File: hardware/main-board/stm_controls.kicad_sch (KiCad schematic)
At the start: 24 parts, among them SW1 SW_SPST, U1 74HC164, U10 MT8816AF1, U11 MT8816AF1, U12 MT8816AF1, U13 AD5263BRUZ200, U14 AD5263BRUZ200, U15 AD5263BRUZ200, U16 AD5263BRUZ200, U17 AD5263BRUZ200, U18 AD5263BRUZ200, U19 AD5263BRUZ200, U2 74HC164, U20 AD5263BRUZ200, U22 STM32F091RCTx, U23 FT232RL, U3 74HC164, U4 MT8816AF1, U5 MT8816AF1, U6 MT8816AF1, U7 MT8816AF1, U8 MT8816AF1, U9 MT8816AF1

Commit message: God is Real, God is Real, Im not kidding this time I wouldn't joke about this
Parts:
- added C1, C10: 10µF, symbol Device:C
- added C2, C3, C4, C5, C9: 100nF, symbol Device:C
- added C6: 10nF, symbol Device:C
- added C7, C8: 1µF, symbol Device:C
- added F1: 500mA, symbol Device:Fuse
- added FB1: 120R, symbol Device:FerriteBead
- added J1: Conn_02x05_Odd_Even, symbol Connector_Generic:Conn_02x05_Odd_Even
- added J2: USB_C_Receptacle_USB2.0_14P, symbol Connector:USB_C_Receptacle_USB2.0_14P
- added J3: Conn_01x02_Pin, symbol Connector:Conn_01x02_Pin
- added R2: 1kΩ, symbol Device:R_US
- added R3: 5.1kΩ, symbol Device:R_US
- added R4: R_US, symbol Device:R_US
- added SW1: SW_SPST, symbol Switch:SW_SPST
- R1: value R_US -> 1kΩ
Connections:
- net GND: now also SW1.1 (A), U22.12 (VSSA), U22.18 (VSS), U22.31 (VSS), U22.47 (VSS), U22.63 (VSS), U23.25 (AGND), C1.2, C10.2, C2.2, C3.2, C4.2, C5.2, C6.2, C7.2, C8.2, C9.2, J1.3 (Pin_3), J1.4 (Pin_4), J2.A1 (GND), J2.A12 (GND), J2.B1 (GND), J2.B12 (GND), J2.S1 (SHIELD), R2.2, R3.2, R4.2; no longer R1.1
- net at U23.15 (USBD+): now also J2.A6 (D+), J2.B6 (D+)
- net at U23.16 (USBD-): now also J2.A7 (D-), J2.B7 (D-)
- net +3.3V: now reaches U23.4 (VCCIO)
- net +3.3V: now also R1.1, U22.1 (VBAT), U22.19 (VDD), U22.32 (VDD), U22.48 (VDDIO2), U22.64 (VDD), C1.1, C2.1, C3.1, C4.1, C5.1, C8.1, FB1.2, J1.7 (Pin_7), J1.8 (Pin_8), SW1.1 (A)
- net +3.3VA: now reaches U22.13 (VDDA)
- net +3.3VA: now also C6.1, C7.1, FB1.1
- net XOSC_IN: now reaches U22.3 (PC14)
- net XOSC_IN: now also J3.2 (Pin_2)
- net XOSC_OUT: now reaches U22.4 (PC15)
- net XOSC_OUT: now also J3.1 (Pin_1)
- net SWDIO: now reaches U22.46 (PA13)
- net SWDIO: now also J1.2 (Pin_2)
- net SWCLK: now reaches U22.49 (PA14)
- net SWCLK: now also J1.6 (Pin_6)
- net at U22.60 (PF11): now also R2.1, SW1.2 (B)
- net +3V3: no longer names the net of U23.20 (VCC)
- net +3V3: now also C10.1, C9.1, F1.2; no longer SW1.1 (A)
- new net: J2.A5 (CC1), R3.1
- new net: J2.B5 (CC2), R4.1
- new net: F1.1, J2.A4 (VBUS), J2.A9 (VBUS), J2.B4 (VBUS), J2.B9 (VBUS)
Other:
- moved on the sheet: SW1, U22, U23

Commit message: fortnite info cache
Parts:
- renumbered C10 to C20, C1 to C21, C9 to C22, C2 to C23, C3 to C24, C4 to C25, C5 to C26, C6 to C27, C7 to C28, C8 to C29, F1 to F3, J1 to J10, J3 to J11, J2 to J9, R3 to R1, R4 to R2, R1 to R3, R2 to R4, SW1 to SW3, SW1 to SW4, U10 to U1, U17 to U14, U18 to U15, U4 to U17, U5 to U18, U14 to U20, U16 to U21, U6 to U23, U7 to U24, U19 to U26, U20 to U27, U8 to U29, U9 to U30, U1 to U33, U23 to U34, U2 to U35, U22 to U36, U3 to U37, U13 to U8, U15 to U9

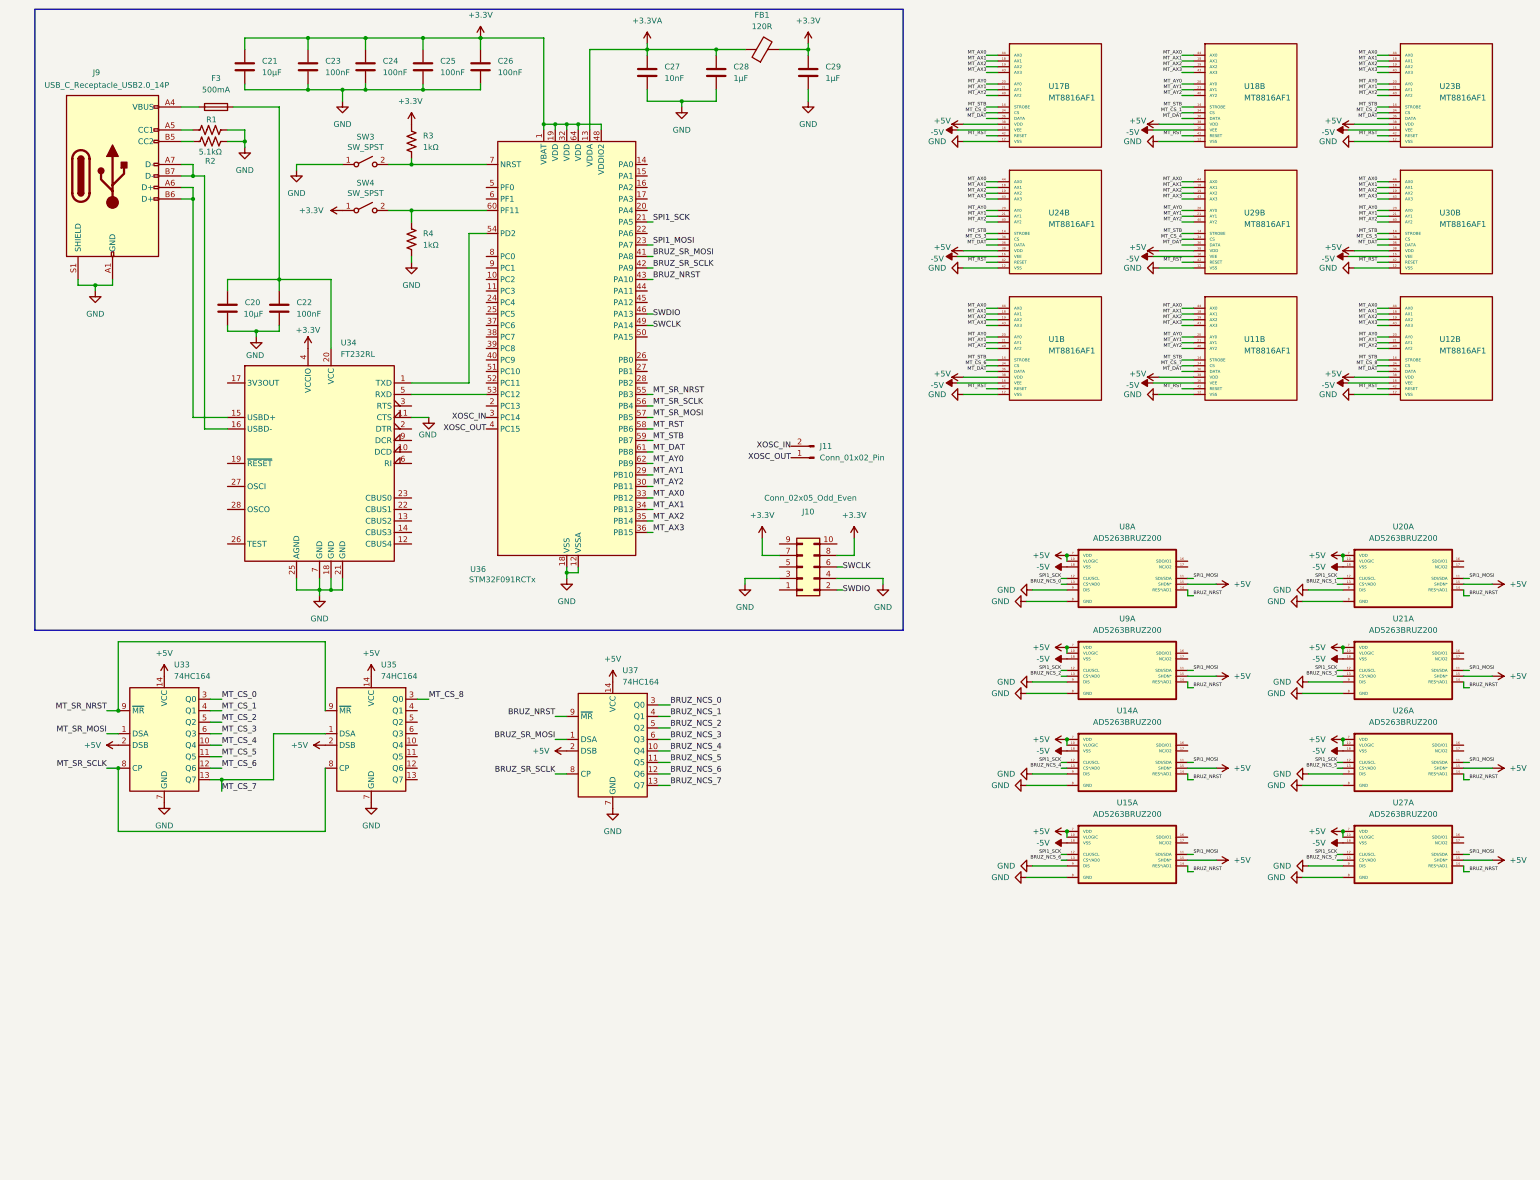
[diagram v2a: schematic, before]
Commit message: Updated Footprints and Controls
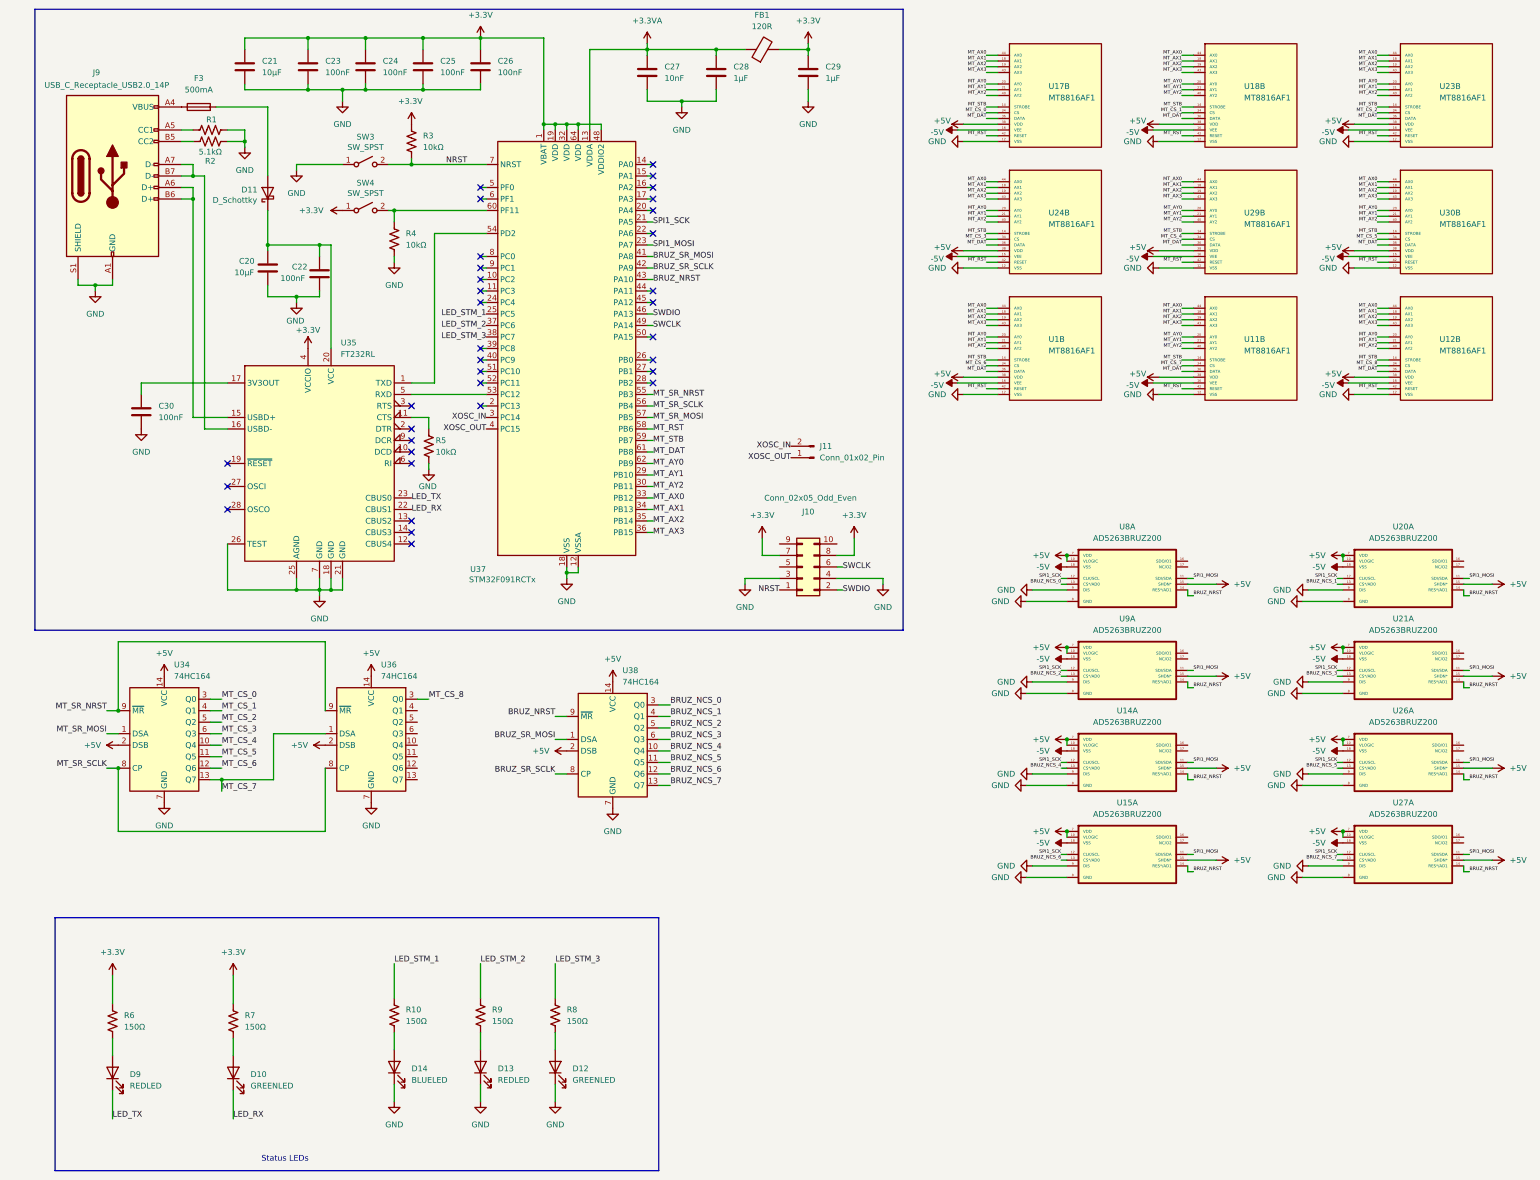
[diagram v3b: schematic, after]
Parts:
- added C30: 100nF, symbol Device:C
- added D10, D12: GREENLED, symbol Device:LED
- added D11: D_Schottky, symbol Device:D_Schottky
- added D13, D9: REDLED, symbol Device:LED
- added D14: BLUELED, symbol Device:LED
- added R10, R6, R7, R8, R9: 150Ω, symbol Device:R_US
- added R5: 10kΩ, symbol Device:R_US
- C20, C21, C22, C23, C24, C25, C26, C27, C28, C29: footprint (none) -> Capacitor_SMD:C_0603_1608Metric_Pad1.08x0.95mm_HandSolder
- F3: footprint (none) -> Fuse:Fuse_0603_1608Metric_Pad1.05x0.95mm_HandSolder
- FB1: footprint (none) -> Inductor_SMD:L_0603_1608Metric_Pad1.05x0.95mm_HandSolder
- J9: footprint (none) -> Connector_USB:USB_C_Receptacle_G-Switch_GT-USB-7010ASV
- R1, R2: footprint (none) -> Resistor_SMD:R_0603_1608Metric_Pad0.98x0.95mm_HandSolder
- R3, R4: value 1kΩ -> 10kΩ; footprint (none) -> Resistor_SMD:R_0603_1608Metric_Pad0.98x0.95mm_HandSolder
- U14, U15, U20, U21, U26, U27, U8, U9: footprint AD5263BRUZ200:SOP65P640X120-24N -> SeniorDesignFP:SOP65P640X120-24N
- U34: renamed from U33; footprint (none) -> Package_SO:SOIC-14_3.9x8.7mm_P1.27mm
- U36: renamed from U35; footprint (none) -> Package_SO:SOIC-14_3.9x8.7mm_P1.27mm
- U38: renamed from U37; footprint (none) -> Package_SO:SOIC-14_3.9x8.7mm_P1.27mm
- renumbered U34 to U35, U36 to U37
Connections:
- net +3.3V: now also R6.1, R7.1
- net GND: now also U35.26 (TEST), C30.2, D12.1 (K), D13.1 (K), D14.1 (K), R5.2; no longer U35.11 (CTS)
- net at C20.1, C22.1, U35.20 (VCC): now also D11.1 (K); no longer F3.2
- net NRST: now reaches R3.2, SW3.2 (B), U37.7 (NRST)
- net NRST: now also J10.1 (Pin_1)
- net at U35.17 (3V3OUT): now also C30.1
- net LED_RX: now reaches U35.22 (CBUS1)
- net LED_RX: now also D10.1 (K)
- net LED_TX: now reaches U35.23 (CBUS0)
- net LED_TX: now also D9.1 (K)
- net LED_STM_1: now reaches U37.25 (PC5)
- net LED_STM_1: now also R10.1
- net LED_STM_2: now reaches U37.37 (PC6)
- net LED_STM_2: now also R9.1
- net LED_STM_3: now reaches U37.38 (PC7)
- net LED_STM_3: now also R8.1
- new net: R5.1, U35.11 (CTS)
- new net: D11.2 (A), F3.2
- new net: D13.2 (A), R9.2
- new net: D10.2 (A), R7.2
- new net: D9.2 (A), R6.2
- new net: D12.2 (A), R8.2
- new net: D14.2 (A), R10.2
- no-connect marks 0 -> 35
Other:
- note added: "Status LEDs"
- moved on the sheet: C20, C22, F3, R4

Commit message: Designated majority of footprints
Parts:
- C30: footprint (none) -> Capacitor_SMD:C_0603_1608Metric_Pad1.08x0.95mm_HandSolder
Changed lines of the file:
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@@
 			)
 		)
-		(property "Footprint" ""
+		(property "Footprint" "Capacitor_SMD:C_0603_1608Metric_Pad1.08x0.95mm_HandSolder"
 			(at 46.6852 105.41 0)
 			(effects

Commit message: Fully filled footprints
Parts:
- D10, D12, D13, D14, D9: footprint (none) -> Diode_SMD:D_0805_2012Metric_Pad1.15x1.40mm_HandSolder
- D11: footprint (none) -> Diode_SMD:D_SOD-123
- J10: footprint (none) -> Connector_PinHeader_1.00mm:PinHeader_2x05_P1.00mm_Horizontal
- J11: footprint (none) -> Connector_PinHeader_1.00mm:PinHeader_1x02_P1.00mm_Horizontal
- R10, R5, R6, R7, R8, R9: footprint (none) -> Resistor_SMD:R_0603_1608Metric_Pad0.98x0.95mm_HandSolder
- SW3, SW4: footprint (none) -> Button_Switch_SMD:SW_SPST_B3U-1100P
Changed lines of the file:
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@@
 			)
 		)
-		(property "Footprint" ""
+		(property "Footprint" "Resistor_SMD:R_0603_1608Metric_Pad0.98x0.95mm_HandSolder"
 			(at 110.236 109.474 90)
 			(effects
@@
 			)
 		)
-		(property "Footprint" ""
+		(property "Footprint" "Diode_SMD:D_SOD-123"
 			(at 73.66 53.34 0)
 			(effects
@@
 			)
 		)
-		(property "Footprint" ""
+		(property "Footprint" "Diode_SMD:D_0805_2012Metric_Pad1.15x1.40mm_HandSolder"
 			(at 120.65 246.38 0)
 			(effects
@@
 			)
 		)
-		(property "Footprint" ""
+		(property "Footprint" "Button_Switch_SMD:SW_SPST_B3U-1100P"
 			(at 95.25 57.15 0)
 			(effects
@@
 			)
 		)
-		(property "Footprint" ""
+		(property "Footprint" "Resistor_SMD:R_0603_1608Metric_Pad0.98x0.95mm_HandSolder"
 			(at 67.056 236.474 90)
 			(effects
@@
 			)
 		)
-		(property "Footprint" ""
+		(property "Footprint" "Button_Switch_SMD:SW_SPST_B3U-1100P"
 			(at 95.25 46.99 0)
 			(effects
@@
 			)
 		)
-		(property "Footprint" ""
+		(property "Footprint" "Diode_SMD:D_0805_2012Metric_Pad1.15x1.40mm_HandSolder"
 			(at 39.37 247.65 0)
 			(effects
@@
 			)
 		)
-		(property "Footprint" ""
+		(property "Footprint" "Diode_SMD:D_0805_2012Metric_Pad1.15x1.40mm_HandSolder"
 			(at 137.16 246.38 0)
 			(effects
@@
 			)
 		)
-		(property "Footprint" ""
+		(property "Footprint" "Diode_SMD:D_0805_2012Metric_Pad1.15x1.40mm_HandSolder"
 			(at 101.6 246.38 0)
 			(effects
@@
 			)
 		)
-		(property "Footprint" ""
+		(property "Footprint" "Resistor_SMD:R_0603_1608Metric_Pad0.98x0.95mm_HandSolder"
 			(at 40.386 236.474 90)
 			(effects
@@
 			)
 		)
-		(property "Footprint" ""
+		(property "Footprint" "Resistor_SMD:R_0603_1608Metric_Pad0.98x0.95mm_HandSolder"
 			(at 102.616 235.204 90)
 			(effects
@@
 			)
 		)
-		(property "Footprint" ""
+		(property "Footprint" "Connector_PinHeader_1.00mm:PinHeader_2x05_P1.00mm_Horizontal"
 			(at 191.77 135.89 0)
 			(effects
@@
 			)
 		)
-		(property "Footprint" ""
+		(property "Footprint" "Resistor_SMD:R_0603_1608Metric_Pad0.98x0.95mm_HandSolder"
 			(at 138.176 235.204 90)
 			(effects
@@
 			)
 		)
-		(property "Footprint" ""
+		(property "Footprint" "Resistor_SMD:R_0603_1608Metric_Pad0.98x0.95mm_HandSolder"
 			(at 121.666 235.204 90)
 			(effects
@@
 			)
 		)
-		(property "Footprint" ""
+		(property "Footprint" "Connector_PinHeader_1.00mm:PinHeader_1x02_P1.00mm_Horizontal"
 			(at 194.31 111.76 0)
 			(effects
@@
 			)
 		)
-		(property "Footprint" ""
+		(property "Footprint" "Diode_SMD:D_0805_2012Metric_Pad1.15x1.40mm_HandSolder"
 			(at 66.04 247.65 0)
 			(effects

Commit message: PCB comps in, and formatted
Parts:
- U1, U11, U12, U17, U18, U23, U24, U29, U30: footprint MT8816AF1:QFP80P1200X1200X120-44N -> SeniorDesignFP:QFP80P1200X1200X120-44N
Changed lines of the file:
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@@
 			)
 		)
-		(property "Footprint" "MT8816AF1:QFP80P1200X1200X120-44N"
+		(property "Footprint" "SeniorDesignFP:QFP80P1200X1200X120-44N"
 			(at 272.034 115.062 0)
 			(effects
@@
 			)
 		)
-		(property "Footprint" "MT8816AF1:QFP80P1200X1200X120-44N"
+		(property "Footprint" "SeniorDesignFP:QFP80P1200X1200X120-44N"
 			(at 358.394 115.062 0)
 			(effects
@@
 			)
 		)
-		(property "Footprint" "MT8816AF1:QFP80P1200X1200X120-44N"
+		(property "Footprint" "SeniorDesignFP:QFP80P1200X1200X120-44N"
 			(at 315.214 87.122 0)
 			(effects
@@
 			)
 		)
-		(property "Footprint" "MT8816AF1:QFP80P1200X1200X120-44N"
+		(property "Footprint" "SeniorDesignFP:QFP80P1200X1200X120-44N"
 			(at 358.394 143.002 0)
 			(effects
@@
 			)
 		)
-		(property "Footprint" "MT8816AF1:QFP80P1200X1200X120-44N"
+		(property "Footprint" "SeniorDesignFP:QFP80P1200X1200X120-44N"
 			(at 272.034 87.122 0)
 			(effects
@@
 			)
 		)
-		(property "Footprint" "MT8816AF1:QFP80P1200X1200X120-44N"
+		(property "Footprint" "SeniorDesignFP:QFP80P1200X1200X120-44N"
 			(at 315.214 115.062 0)
 			(effects
@@
 			)
 		)
-		(property "Footprint" "MT8816AF1:QFP80P1200X1200X120-44N"
+		(property "Footprint" "SeniorDesignFP:QFP80P1200X1200X120-44N"
 			(at 315.214 143.002 0)
 			(effects
@@
 			)
 		)
-		(property "Footprint" "MT8816AF1:QFP80P1200X1200X120-44N"
+		(property "Footprint" "SeniorDesignFP:QFP80P1200X1200X120-44N"
 			(at 358.394 87.122 0)
 			(effects
@@
 			)
 		)
-		(property "Footprint" "MT8816AF1:QFP80P1200X1200X120-44N"
+		(property "Footprint" "SeniorDesignFP:QFP80P1200X1200X120-44N"
 			(at 272.034 143.002 0)
 			(effects
